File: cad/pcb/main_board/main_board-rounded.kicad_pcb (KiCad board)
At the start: 2 copper layers, 120 x 100 mm, 72 parts, among them J1 USB_B_Micro, SW1 SW_DIP_x02, SW2 SW_DIP_x01, U1 STM32F401R_B-C_Tx, U2 TLV75533PDRVR

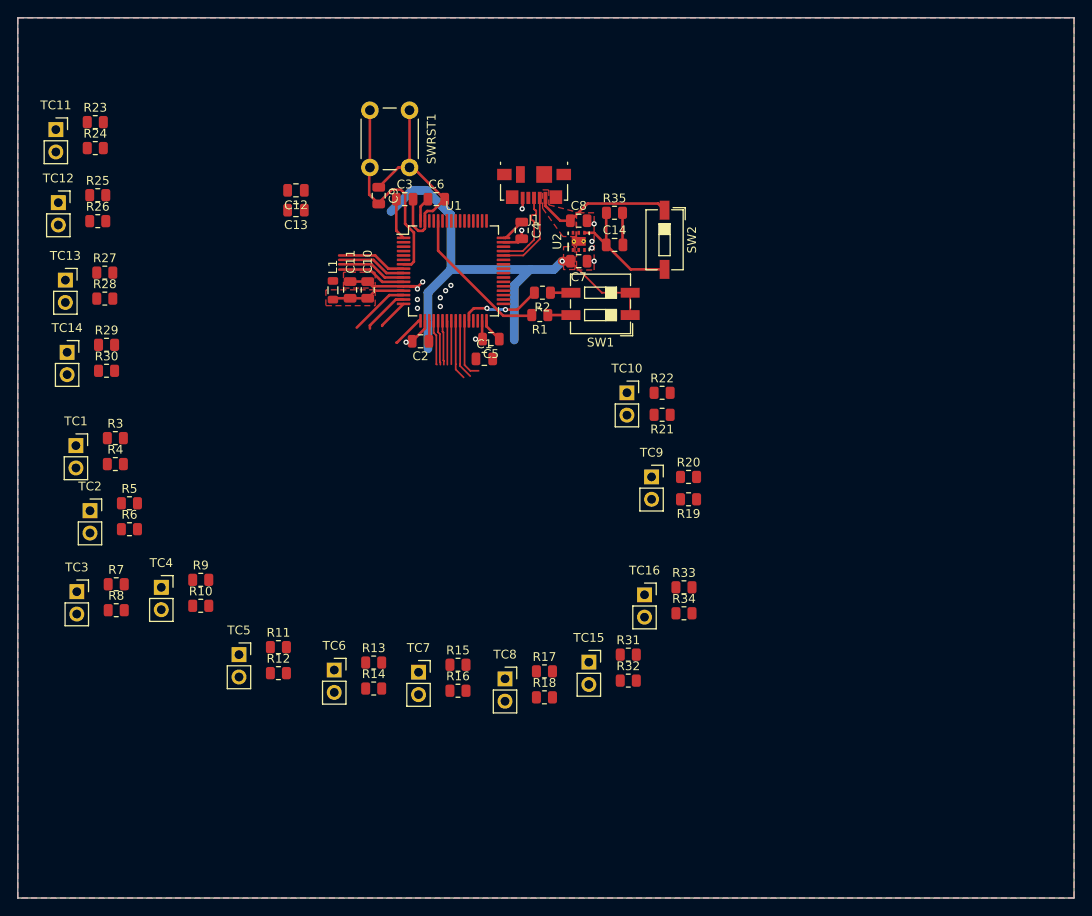
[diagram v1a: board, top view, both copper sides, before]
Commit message: Aligning Thermo Couple Resistors
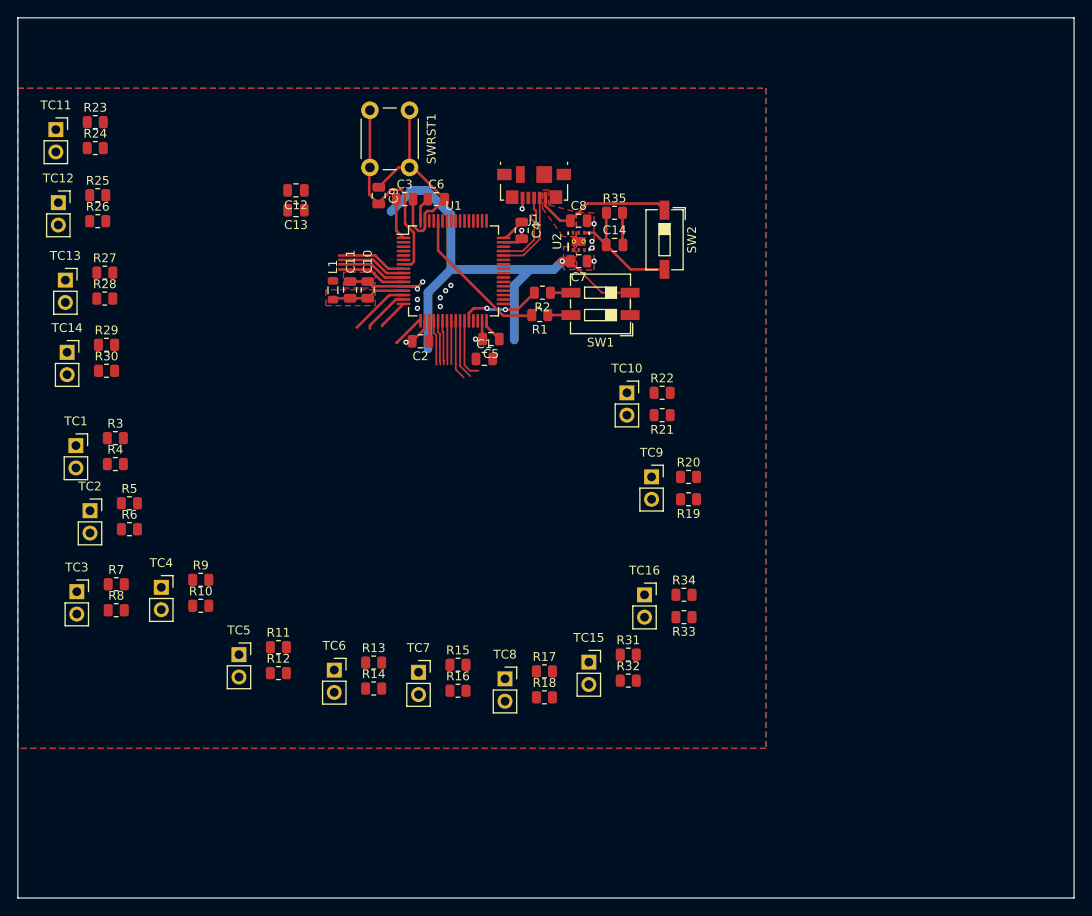
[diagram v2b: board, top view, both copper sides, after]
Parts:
- moved R33 3.39 mm to (135.7, 92.1), turned to 180 degrees
- moved R34 2.10 mm to (135.7, 89.5)
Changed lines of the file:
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@@
 	)
 	(footprint "Resistor_SMD:R_0805_2012Metric"
+		(locked yes)
 		(layer "F.Cu")
-		(at 135.68 88.7)
+		(at 135.68 92.09 180)
 		(descr "Resistor SMD 0805 (2012 Metric), square (rectangular) end terminal, IPC_7351 nominal, (Body size source: IPC-SM-782 page 72, https://www.pcb-3d.com/wordpress/wp-content/uploads/ipc-sm-782a_amendment_1_and_2.pdf), generated with kicad-footprint-generator")
 		(tags "resistor")
 		(property "Reference" "R33"
-			(at 0 -1.65 0)
+			(at 0 -1.65 360)
 			(layer "F.SilkS")
 			(effects
@@
 		)
 		(property "Value" "10kR"
-			(at 0 1.65 0)
+			(at 0 1.65 360)
 			(layer "F.Fab")
 			(effects
@@
 		)
 		(property "Footprint" "Resistor_SMD:R_0805_2012Metric"
-			(at 0 0 0)
+			(at 0 0 360)
 			(layer "F.Fab")
 			(hide yes)
@@
 		)
 		(property "Datasheet" ""
-			(at 0 0 0)
+			(at 0 0 360)
 			(layer "F.Fab")
 			(hide yes)
@@
 		)
 		(property "Description" ""
-			(at 0 0 0)
+			(at 0 0 360)
 			(layer "F.Fab")
 			(hide yes)
@@
 		(attr smd)
 		(fp_line
-			(start -0.227064 -0.735)
-			(end 0.227064 -0.735)
+			(start -0.227064 0.735)
+			(end 0.227064 0.735)
 			(stroke
 				(width 0.12)
@@
 		)
 		(fp_line
-			(start -0.227064 0.735)
-			(end 0.227064 0.735)
+			(start -0.227064 -0.735)
+			(end 0.227064 -0.735)
 			(stroke
 				(width 0.12)
@@
 		)
 		(fp_line
-			(start -1.68 -0.95)
-			(end 1.68 -0.95)
+			(start 1.68 0.95)
+			(end -1.68 0.95)
 			(stroke
 				(width 0.05)
@@
 		)
 		(fp_line
-			(start -1.68 0.95)
-			(end -1.68 -0.95)
+			(start 1.68 -0.95)
+			(end 1.68 0.95)
 			(stroke
 				(width 0.05)
@@
 		)
 		(fp_line
-			(start 1.68 -0.95)
-			(end 1.68 0.95)
+			(start -1.68 0.95)
+			(end -1.68 -0.95)
 			(stroke
 				(width 0.05)
@@
 		)
 		(fp_line
-			(start 1.68 0.95)
-			(end -1.68 0.95)
+			(start -1.68 -0.95)
+			(end 1.68 -0.95)
 			(stroke
 				(width 0.05)
@@
 		)
 		(fp_line
-			(start -1 -0.625)
-			(end 1 -0.625)
+			(start 1 0.625)
+			(end -1 0.625)
 			(stroke
 				(width 0.1)
@@
 		)
 		(fp_line
-			(start -1 0.625)
-			(end -1 -0.625)
+			(start 1 -0.625)
+			(end 1 0.625)
 			(stroke
 				(width 0.1)
@@
 		)
 		(fp_line
-			(start 1 -0.625)
-			(end 1 0.625)
+			(start -1 0.625)
+			(end -1 -0.625)
 			(stroke
 				(width 0.1)
@@
 		)
 		(fp_line
-			(start 1 0.625)
-			(end -1 0.625)
+			(start -1 -0.625)
+			(end 1 -0.625)
 			(stroke
 				(width 0.1)
@@
 		)
 		(fp_text user "${REFERENCE}"
-			(at 0 0 0)
+			(at 0 0 360)
 			(layer "F.Fab")
 			(effects
@@
 		)
 		(pad "1" smd roundrect
-			(at -0.9125 0)
+			(at -0.9125 0 180)
 			(size 1.025 1.4)
 			(layers "F.Cu" "F.Paste" "F.Mask")
@@
 		)
 		(pad "2" smd roundrect
-			(at 0.9125 0)
+			(at 0.9125 0 180)
 			(size 1.025 1.4)
 			(layers "F.Cu" "F.Paste" "F.Mask")
@@
 	)
 	(footprint "Resistor_SMD:R_0805_2012Metric"
+		(locked yes)
 		(layer "F.Cu")
-		(at 133.2 69.1 180)
+		(at 133.2 69.14 180)
 		(descr "Resistor SMD 0805 (2012 Metric), square (rectangular) end terminal, IPC_7351 nominal, (Body size source: IPC-SM-782 page 72, https://www.pcb-3d.com/wordpress/wp-content/uploads/ipc-sm-782a_amendment_1_and_2.pdf), generated with kicad-footprint-generator")
 		(tags "resistor")
@@
 	)
 	(footprint "Resistor_SMD:R_0805_2012Metric"
+		(locked yes)
 		(layer "F.Cu")
-		(at 135.68 91.65)
+		(at 135.68 89.55)
 		(descr "Resistor SMD 0805 (2012 Metric), square (rectangular) end terminal, IPC_7351 nominal, (Body size source: IPC-SM-782 page 72, https://www.pcb-3d.com/wordpress/wp-content/uploads/ipc-sm-782a_amendment_1_and_2.pdf), generated with kicad-footprint-generator")
 		(tags "resistor")
@@
 	)
 	(footprint "Connector_PinSocket_2.54mm:PinSocket_1x02_P2.54mm_Vertical"
+		(locked yes)
 		(layer "F.Cu")
 		(at 132 76.16)
@@
 	)
 	(footprint "Resistor_SMD:R_0805_2012Metric"
+		(locked yes)
 		(layer "F.Cu")
 		(at 136.2 78.7 180)
@@
 	)
 	(footprint "Connector_PinSocket_2.54mm:PinSocket_1x02_P2.54mm_Vertical"
+		(locked yes)
 		(layer "F.Cu")
 		(at 129.2 66.6)
@@
 	)
 	(footprint "Connector_PinSocket_2.54mm:PinSocket_1x02_P2.54mm_Vertical"
+		(locked yes)
 		(layer "F.Cu")
 		(at 131.2 89.55)
@@
 	)
 	(footprint "Resistor_SMD:R_0805_2012Metric"
+		(locked yes)
 		(layer "F.Cu")
 		(at 136.2 76.16)
@@
 	)
 	(footprint "Resistor_SMD:R_0805_2012Metric"
+		(locked yes)
 		(layer "F.Cu")
 		(at 133.2 66.6)
@@
 		(min_thickness 0.25)
 		(filled_areas_thickness no)
-		(fill yes
+		(fill
 			(thermal_gap 0.5)
 			(thermal_bridge_width 0.5)
@@
 		(polygon
 			(pts
-				(xy 60 24) (xy 180 24) (xy 180 124) (xy 60 124)
+				(xy 60 32) (xy 145 32) (xy 145 107) (xy 60 107)
 			)
 		)
 	)
 	(group ""
-		(members "31afeda4-1593-44cb-9129-6b21c08b6adb" "427ee41f-a357-44f8-9dba-adad1c672cad"
-			"d85dd901-91d6-40af-9252-312ea06b588e"
-		)
-	)
-	(group ""
-		(members "46814b23-cd12-46bc-b0a4-fabf5e51e06c" "6f7a870e-ff29-462a-85a6-d36b60906101"
-			"b97c63d1-b2d7-45e7-a0da-a3778c0f9738"
-		)
-	)
-	(group ""
-		(members "1c210a3b-0570-422f-9ec7-15f9d3b97d16" "6b90acd6-b131-4efe-9064-a7ad349010d5"
-			"9dcabe5c-1d5f-48c9-bc23-359d4c856da5"
-		)
-	)
-	(group ""
 		(members "16c7479d-4a3d-4b50-8e7d-80acae4c9763" "255e9168-3ef2-4268-ae86-c273014f0e93"
 			"2836aa6a-0978-4faf-8f8f-6a046b5207da" "344683fa-2142-48b3-bd64-cf76fe877eaf"
@@
 		)
 	)
-	(group ""
-		(members "01e5d53c-a683-4f19-b749-21cb43a6ced5" "40f843e0-df90-4f76-8b15-b7d38f1f3ba0"
-			"d75538e7-73eb-463d-a557-a998c6576203"
-		)
-	)
-	(group ""
-		(members "6aa434d5-6fa7-4525-8ee6-a5af06f9f0f1" "edb75592-19cf-4706-9fdc-98ac9f932c6b"
-			"fec9de97-5558-4ec0-a387-c3fc068a35d3"
-		)
-	)
-	(group ""
-		(members "09a5c6b3-faac-451b-8eee-eb6ccf3b0a75" "11b83bbc-2b9a-4d7e-afc9-491e8d90665b"
-			"ccb01b46-bdce-4024-a3ee-9190b1390aac"
-		)
-	)
-	(group ""
-		(members "a7cd57b7-22ff-40fd-a35f-40142ddeee62" "ef2a0d5d-c7fc-4335-9edd-60033ea77d89"
-			"f1bb86d2-6883-4c79-be0b-932643962223"
-		)
-	)
-	(group ""
-		(members "6d46ddd8-f34d-40b9-8b31-774572d9709e" "71289d33-85de-403c-be4d-b8246bcc9065"
-			"f14fad15-39fc-4088-9636-a7ef6007ec8f"
-		)
-	)
-	(group ""
-		(members "274e5ff0-9b9c-4686-a580-f35096b92f4b" "9ed3548e-44e8-4789-9e55-7646b9741492"
-			"c825f2e3-9390-4713-9a27-a1f3c3082043"
-		)
-	)
-	(group ""
-		(members "5f9a2a51-b7c5-4628-8caf-18c4c4a8e760" "7cba04c7-6649-4d5d-bc20-6e8ad670be18"
-			"eec16172-bc19-49a0-ba79-7c27c21aa403"
-		)
-	)
-	(group ""
-		(members "790dcce9-b288-453d-8c5a-9d9c38e586b3" "815109c0-e9b8-4263-98dd-8c3c4aff43b9"
-			"b5d505cc-43ce-4a79-960c-f421b62d5716"
-		)
-	)
-	(group ""
-		(members "13c404a8-3e85-41bf-83be-c1c43acc30b8" "661d339d-4ac7-4fe4-9edc-27ed40f77a3b"
-			"a13d5517-74ae-4f2b-96dc-14ebb24fb5a3"
-		)
-	)
-	(group ""
-		(members "43b86b4b-8488-4383-b4de-6341da0d5042" "96ae6878-c265-47cd-8b05-bdc719c2d008"
-			"a89335e0-06dc-4e6c-b1db-4e701603967d"
-		)
-	)

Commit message: Hooking up ThermoCouple pins first layout of TCs
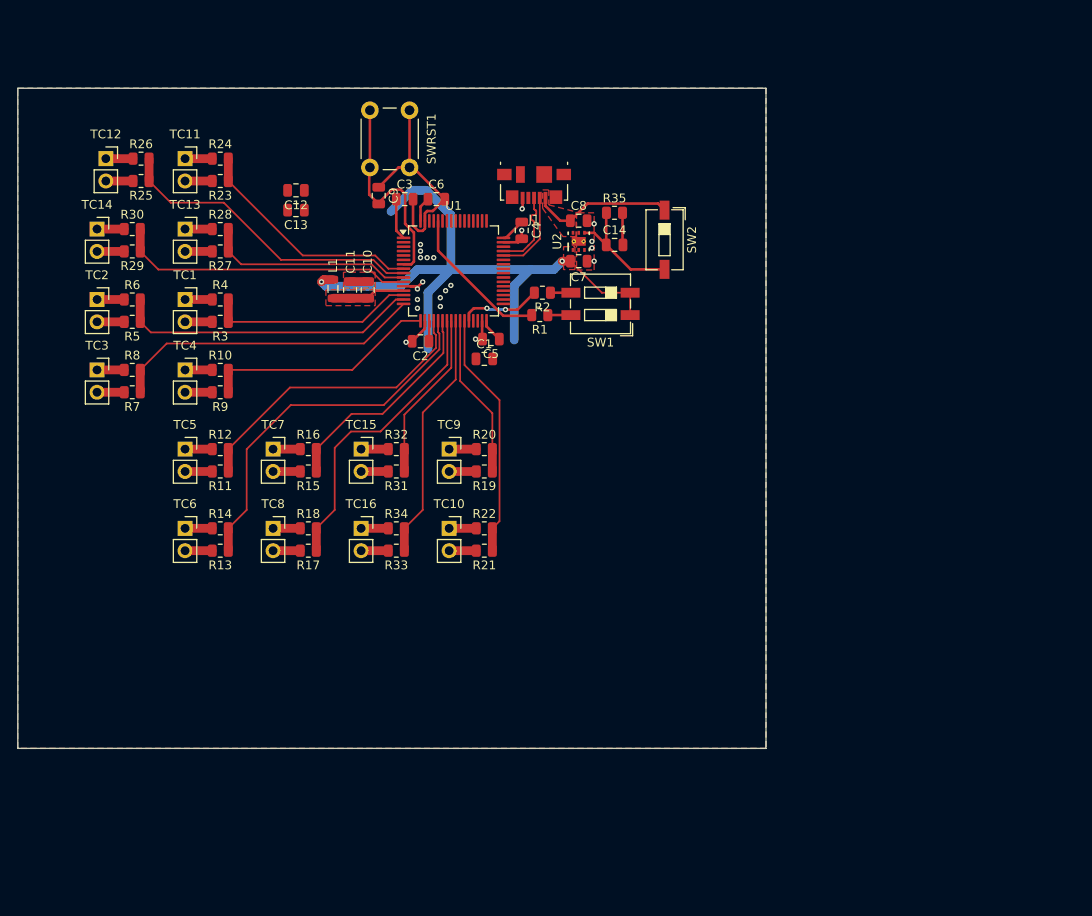
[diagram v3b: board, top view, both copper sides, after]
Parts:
- moved R32 37.2 mm to (103.0, 73.0)
- moved TC15 35.4 mm to (99.0, 73.0)
- moved R31 33.6 mm to (103.0, 75.5), turned to 180 degrees
- moved R33 33.5 mm to (103.0, 84.5)
- moved R34 33.5 mm to (103.0, 82.0)
- moved TC16 33.1 mm to (99.0, 82.0)
- moved R18 33.0 mm to (93.0, 82.0)
- moved R16 32.3 mm to (93.0, 73.0)
- moved TC8 31.4 mm to (89.0, 82.0)
- moved TC7 30.3 mm to (89.0, 73.0)
- moved R17 30.1 mm to (93.0, 84.5), turned to 180 degrees
- moved R15 27.8 mm to (93.0, 75.5), turned to 180 degrees
- moved R8 27.4 mm to (73.0, 64.0)
- moved R10 26.9 mm to (83.0, 64.0)
- moved R12 26.3 mm to (83.0, 73.0)
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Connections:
- U1 pad 12: VSS -> VSSA
- U2 pad 2: VSS -> unconnected-(U2-NC-Pad2)
- U2 pad 5: VSS -> unconnected-(U2-NC-Pad5)
- U2 pad V: VSS -> (no net)
- U2 pad VSS: VSS -> (no net)
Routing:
- net VSSA: track 0.00 -> 51.9 mm
- net /MCU/ADC_IN5: track 5.08 -> 42.3 mm
- net /MCU/ADC_IN2: track 3.50 -> 35.6 mm
- net /MCU/ADC_IN7: track 5.00 -> 34.3 mm
- net /MCU/ADC_IN1: track 5.40 -> 34.5 mm
- net /MCU/ADC_IN4: track 5.12 -> 34.1 mm
- net /MCU/ADC_IN11: track 7.95 -> 35.8 mm
- net /MCU/ADC_IN13: track 7.90 -> 33.9 mm
- net /MCU/ADC_IN3: track 3.78 -> 26.7 mm
- net /MCU/ADC_IN15: track 6.80 -> 28.5 mm
- net /MCU/ADC_IN9: track 6.89 -> 28.1 mm
- net /MCU/ADC_IN6: track 5.04 -> 25.2 mm
- net /MCU/ADC_IN10: track 7.95 -> 26.6 mm
- net VDD: track 74.2 -> 91.3 mm, vias 1 -> 2
- net /MCU/ADC_IN0: track 6.86 -> 23.7 mm
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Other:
- board size 120 x 100 mm -> 85 x 75 mm

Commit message: Adding JTAG Interface + POGO Pads
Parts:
- added C15: C, Capacitor_SMD:C_0805_2012Metric, F.Cu at (94.5, 34.0)
- added J2: Conn_ARM_JTAG_SWD_10, local:POGO_JTAG_SWD, F.Cu at (93.5, 41.0)
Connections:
- U1 pad 46: unconnected-(U1-PA13-Pad46) -> Net-(J2-SWDIO/TMS)
- U1 pad 49: unconnected-(U1-PA14-Pad49) -> Net-(J2-SWCLK/TCK)
- U1 pad 50: unconnected-(U1-PA15-Pad50) -> Net-(J2-NC/TDI)
- U1 pad 55: unconnected-(U1-PB3-Pad55) -> Net-(J2-SWO/TDO)
- U1 pad 56: unconnected-(U1-PB4-Pad56) -> Net-(J2-~{RESET})
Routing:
- net Net-(J2-SWCLK/TCK): track 0.00 -> 37.4 mm, vias 0 -> 2
- net Net-(J2-SWDIO/TMS): track 0.00 -> 37.0 mm, vias 0 -> 2
- net Net-(J2-SWO/TDO): track 0.00 -> 30.4 mm, vias 0 -> 2
- net Net-(J2-NC/TDI): track 0.00 -> 29.2 mm, vias 0 -> 2
- net Net-(J2-~{RESET}): track 0.00 -> 22.6 mm, vias 0 -> 2
- net VSS: track 41.7 -> 58.1 mm, vias 21 -> 20
- net VDD: track 91.3 -> 100.6 mm
- net Net-(J2-GNDDetect): track 0.00 -> 2.23 mm
